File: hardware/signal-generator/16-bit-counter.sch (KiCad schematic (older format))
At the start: 20 parts

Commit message: [Signal Generator] Layout microcontroller and allocate its pins
The microcontroller is the brains of the function generator system - it
is responsible for controlling the DDS signal generator system, as well
as the LCD module which provides the user interface. The specific
microcontroller used in this project is the ATmega2561-16AU from the
megaAVR uC family. The reasons I have picked this particular part are
the following:
- I am familiar with the AVR uC structure;
- it provides more SRAM memory (8 kB) than other MCUs of the same family;
- it has fewer pins (and therefore peripherals) than the ATmega2560.
Only a fraction of the available peripheral pins of the ATmega2561 have
been utilized in the current design. The remaining port pins (which are
internally connected to useful peripherals such as JTAG, XMEM, etc.)
are connected to pin header connectors and are meant for
upgrading/modifying the system as a whole by including additional
external circuitry. The ATmega2561's SPI port is also connected to a
similar pin header connector which allows the uC to play the role of an
SPI slave device.
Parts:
- removed U? (x2): 74HC30, Housings_SOIC:SOIC-14_3.9x8.7mm_Pitch1.27mm, symbol MY_74xx:74HC30
- removed U? (x2): 74HC4040, Housings_SOIC:SOIC-16_3.9x9.9mm_Pitch1.27mm, symbol MY_74xx:74HC4040
- removed U? (x10): 74HC08, Housings_SOIC:SOIC-14_3.9x8.7mm_Pitch1.27mm, symbol MY_74xx:74HC08
- added U? (x2): 74HC4040, Housings_SOIC:SOIC-16_3.9x9.9mm_Pitch1.27mm, symbol ulib_MY_74xx:74HC4040
- added U? (x2): 74HC30, Housings_SOIC:SOIC-14_3.9x8.7mm_Pitch1.27mm, symbol ulib_MY_74xx:74HC30
- added U? (x10): 74HC08, Housings_SOIC:SOIC-14_3.9x8.7mm_Pitch1.27mm, symbol ulib_MY_74xx:74HC08

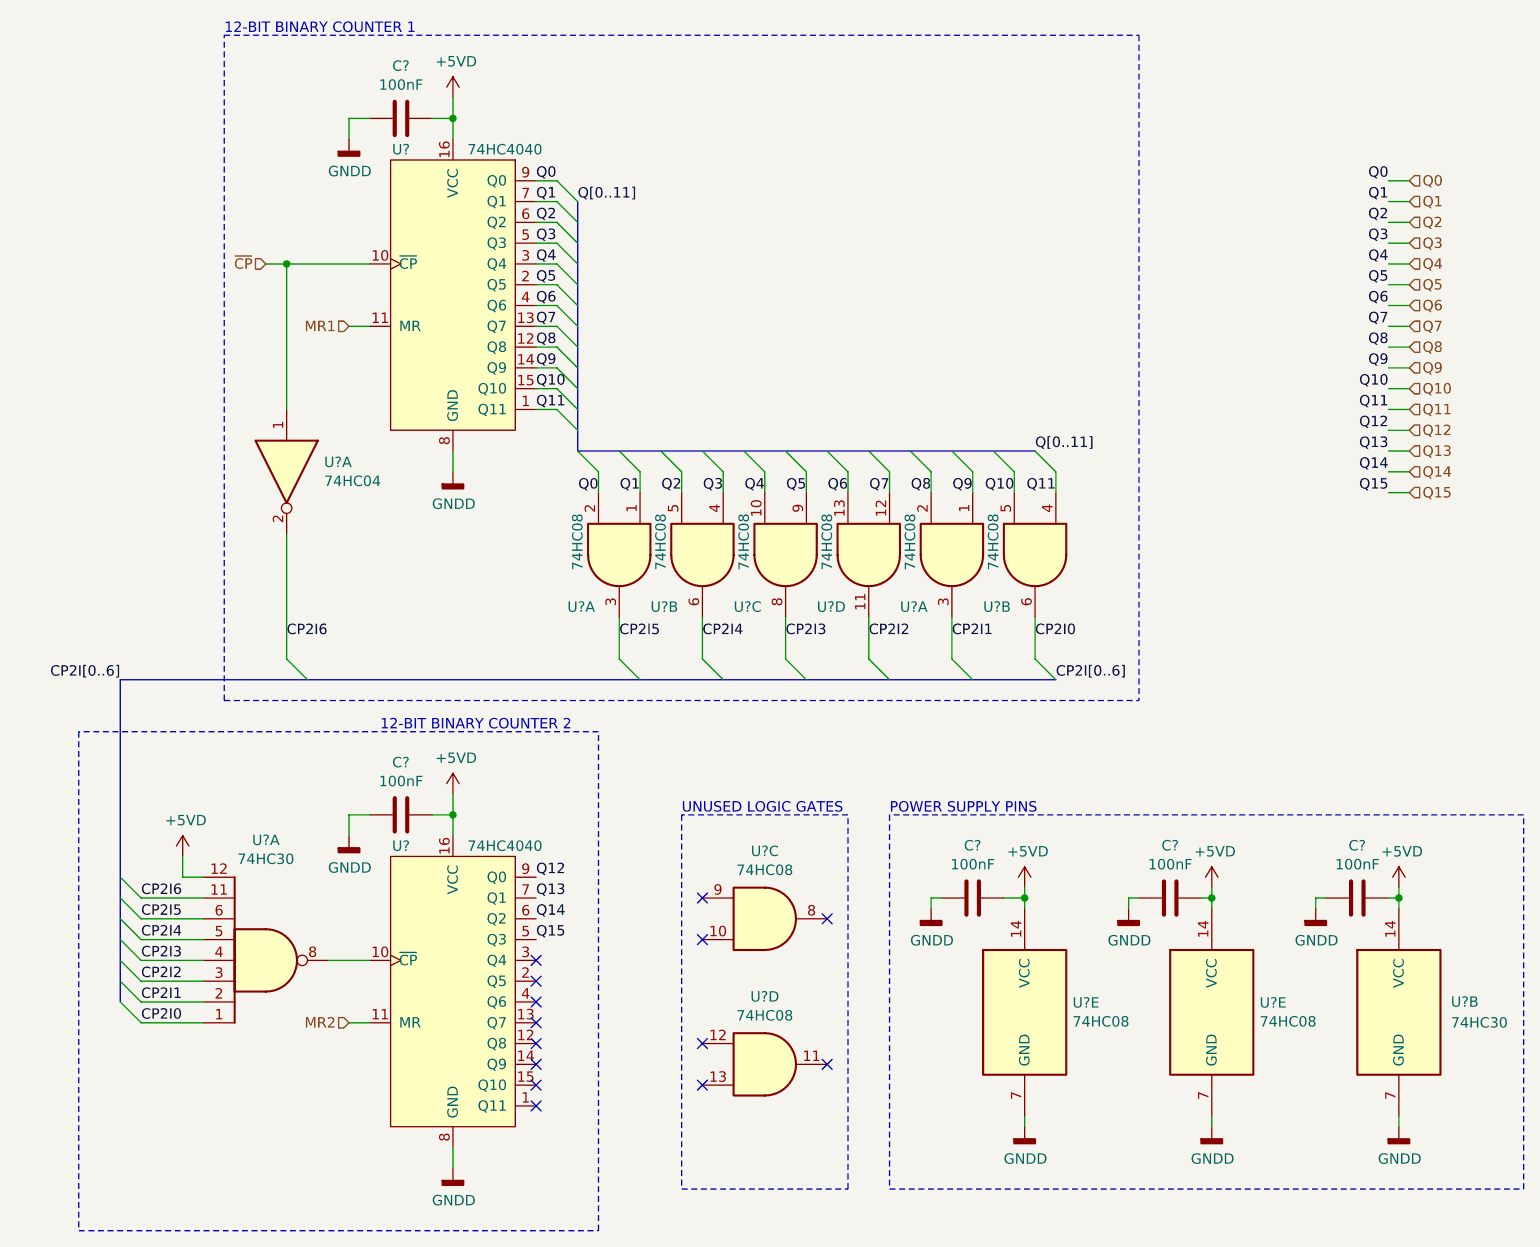
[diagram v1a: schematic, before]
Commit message: [Signal Generator] Place unused logic gates and logic IC supplies
Both of these elements can be located on the main project sheet
('signal-generator.sch').
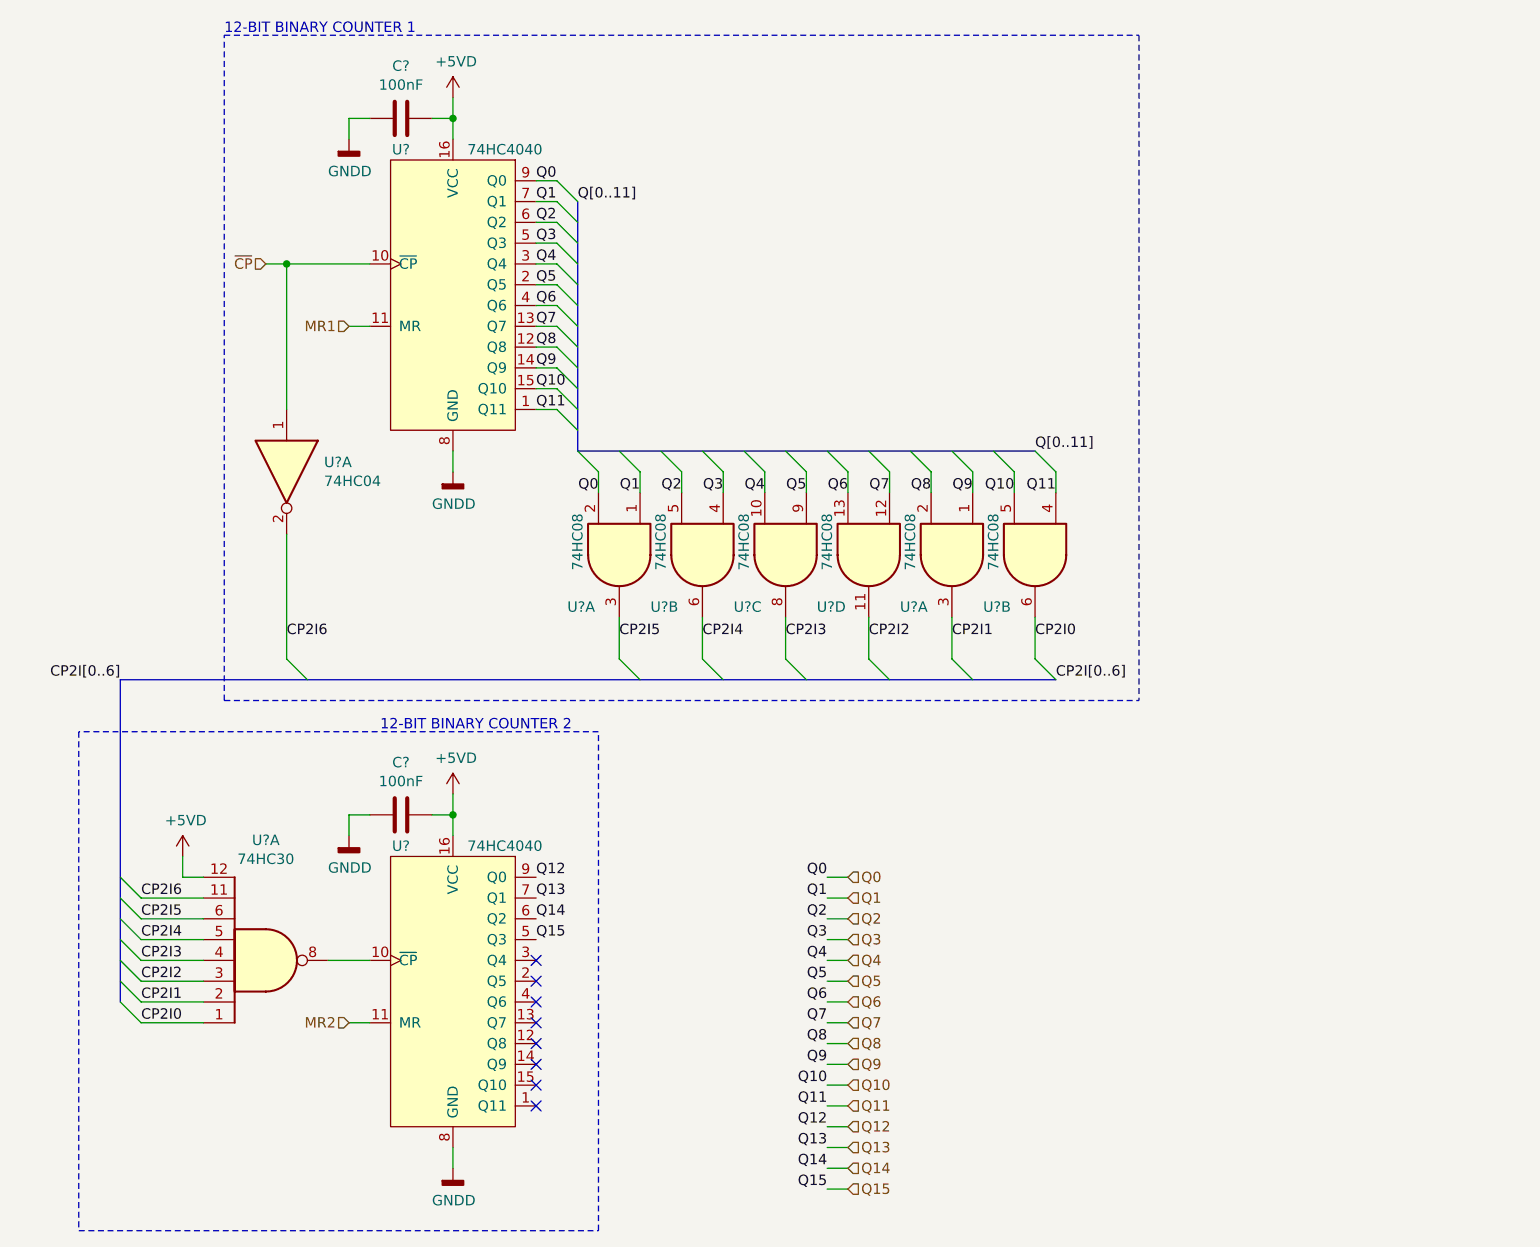
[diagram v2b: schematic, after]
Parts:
- removed C? (x3): 100nF, symbol Device:C
- removed U?: 74HC30, Housings_SOIC:SOIC-14_3.9x8.7mm_Pitch1.27mm, symbol ulib_MY_74xx:74HC30
- removed U? (x4): 74HC08, Housings_SOIC:SOIC-14_3.9x8.7mm_Pitch1.27mm, symbol ulib_MY_74xx:74HC08
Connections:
- no-connect marks 14 -> 8
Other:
- note removed: "POWER SUPPLY PINS"
- note removed: "UNUSED LOGIC GATES"

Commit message: [Signal Generator] Implement +3.3VD line with TC1017 voltage regulator
Up until now, the +3.3VD line was implemented using the L78L33 linear
voltage regulator. However, the latter has a dropout voltage of 2V which
means that the L78L33 cannot output a stable +3.3V from a +5V input.

To solve the aforementioned problem the TC1017 LDO voltage regulator has
replaced the L78L33. The former has a low dropout voltage of 180mV (typ.) at
100mA load current.
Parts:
- C? (x2): footprint (none) -> Capacitors_SMD:C_1206_HandSoldering
- U?: footprint (none) -> Housings_SOIC:SOIC-14_3.9x8.7mm_Pitch1.27mm
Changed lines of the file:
@@
 F 0 "C?" V 3748 4600 50  0000 C CNN
 F 1 "100nF" V 3839 4600 50  0000 C CNN
-F 2 "" H 4038 4450 50  0001 C CNN
+F 2 "Capacitors_SMD:C_1206_HandSoldering" H 4038 4450 50  0001 C CNN
 F 3 "~" H 4000 4600 50  0001 C CNN
 	1    4000 4600
@@
 	3750 4600 3750 4700
 $Comp
-L power:GNDD #PWR?
+L power:GNDD #PWR0172
 U 1 1 5DBB9690
 P 3750 4700
-F 0 "#PWR?" H 3750 4450 50  0001 C CNN
+F 0 "#PWR0172" H 3750 4450 50  0001 C CNN
 F 1 "GNDD" H 3754 4545 50  0000 C CNN
 F 2 "" H 3750 4700 50  0001 C CNN
@@
 Connection ~ 4250 4600
 $Comp
-L power:+5VD #PWR?
+L power:+5VD #PWR0173
 U 1 1 5DBB9DC1
 P 4250 4500
-F 0 "#PWR?" H 4250 4350 50  0001 C CNN
+F 0 "#PWR0173" H 4250 4350 50  0001 C CNN
 F 1 "+5VD" H 4265 4673 50  0000 C CNN
 F 2 "" H 4250 4500 50  0001 C CNN
@@
 F 0 "C?" V 3748 1250 50  0000 C CNN
 F 1 "100nF" V 3839 1250 50  0000 C CNN
-F 2 "" H 4038 1100 50  0001 C CNN
+F 2 "Capacitors_SMD:C_1206_HandSoldering" H 4038 1100 50  0001 C CNN
 F 3 "~" H 4000 1250 50  0001 C CNN
 	1    4000 1250
@@
 	3750 1250 3750 1350
 $Comp
-L power:GNDD #PWR?
+L power:GNDD #PWR0174
 U 1 1 5DBBB94E
 P 3750 1350
-F 0 "#PWR?" H 3750 1100 50  0001 C CNN
+F 0 "#PWR0174" H 3750 1100 50  0001 C CNN
 F 1 "GNDD" H 3754 1195 50  0000 C CNN
 F 2 "" H 3750 1350 50  0001 C CNN
@@
 Connection ~ 4250 1250
 $Comp
-L power:+5VD #PWR?
+L power:+5VD #PWR0175
 U 1 1 5DBBC2D6
 P 4250 1150
-F 0 "#PWR?" H 4250 1000 50  0001 C CNN
+F 0 "#PWR0175" H 4250 1000 50  0001 C CNN
 F 1 "+5VD" H 4265 1323 50  0000 C CNN
 F 2 "" H 4250 1150 50  0001 C CNN
@@
 	4250 2850 4250 2950
 $Comp
-L power:GNDD #PWR?
+L power:GNDD #PWR0176
 U 1 1 5DBBD1F3
 P 4250 2950
-F 0 "#PWR?" H 4250 2700 50  0001 C CNN
+F 0 "#PWR0176" H 4250 2700 50  0001 C CNN
 F 1 "GNDD" H 4254 2795 50  0000 C CNN
 F 2 "" H 4250 2950 50  0001 C CNN
@@
 	4250 6200 4250 6300
 $Comp
-L power:GNDD #PWR?
+L power:GNDD #PWR0177
 U 1 1 5DBBE1A2
 P 4250 6300
-F 0 "#PWR?" H 4250 6050 50  0001 C CNN
+F 0 "#PWR0177" H 4250 6050 50  0001 C CNN
 F 1 "GNDD" H 4254 6145 50  0000 C CNN
 F 2 "" H 4250 6300 50  0001 C CNN
@@
 	2950 4900 2950 4800
 $Comp
-L power:+5VD #PWR?
+L power:+5VD #PWR0178
 U 1 1 5DBCA96D
 P 2950 4800
-F 0 "#PWR?" H 2950 4650 50  0001 C CNN
+F 0 "#PWR0178" H 2950 4650 50  0001 C CNN
 F 1 "+5VD" H 2965 4973 50  0000 C CNN
 F 2 "" H 2950 4800 50  0001 C CNN
@@
 F 0 "U?" V 3404 3130 50  0000 L CNN
 F 1 "74HC04" V 3495 3130 50  0000 L CNN
-F 2 "" H 3450 2950 50  0001 C CNN
+F 2 "Housings_SOIC:SOIC-14_3.9x8.7mm_Pitch1.27mm" H 3450 2950 50  0001 C CNN
 F 3 "https://assets.nexperia.com/documents/data-sheet/74HC_HCT04.pdf" H 3450 2950 50  0001 C CNN
 	1    3450 2950
